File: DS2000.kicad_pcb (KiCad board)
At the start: 4 copper layers, 72 x 46 mm, 58 parts, among them J1 USB-C, J3 USB wire, SW1 MUTE, SW2 DEAFEN, SW3 DISCONNECT, U1 USBLC6-2SC6, U2 AP2112K-3.3, U3 RP2350A, U4 W25Q32JVSS, U5 74AHCT1G125, Y1 12MHz

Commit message: feat: cost-down for one-sided JLC assembly
Move every assembled part to the top side so JLC can assemble the board
with Economic PCBA, and swap parts that have a JLC basic (no feeder fee)
or cheaper drop-in equivalent.

- remove the USB-C receptacle (J1) and its CC resistors (R1, R2): the USB
  cable is soldered to J3, which now feeds +5V directly
- remove the PTC fuse (F1): the host port limits the current
- D1/D2: SK6812MINI-E reverse-mount (bottom) -> WS2812B-2020-V6 on the
  top, inside the Choc V1 LED window; no more board cut-outs
- C21/C22 move to the top, between the keys, under the keycap overhang
- U2: AP2112K-3.3 (SOT-23-5) -> XC6206P332MR (SOT-23-3, basic)
- Y1: ABM8-272-T3 -> YXC X322512MSB4SI (basic), C17/C18 15p -> 33p
- C3-C5 -> CL05A475MP5NRNC (basic), R5 -> 0402WGF330JTCE (basic)
- U1 -> UMW USBLC6-2SC6, U4 -> W25Q16JVSSIQ (2 MB, same footprint)
- the changed nets rerouted with Freerouting, existing tracks locked
- STEP model for the WS2812B-2020, docs and renders updated

Co-Authored-By: Claude Opus 5.5 <noreply@anthropic.com>
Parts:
- removed F1: 500mA hold, Fuse:Fuse_1206_3216Metric
- removed J1: USB-C, Connector_USB:USB_C_Receptacle_HRO_TYPE-C-31-M-12
- removed R1, R2: 5.1k, Resistor_SMD:R_0402_1005Metric
- C17, C18: value 15p -> 33p
- C21, C22: moved to F.Cu
- D1, D2: value SK6812MINI-E -> WS2812B-2020; footprint LED_SMD:LED_SK6812MINI-E_3.2x2.8mm_P1.5mm_ReverseMount -> LED_SMD:LED_WS2812B-2020_PLCC4_2.0x2.0mm; moved to F.Cu
- U2: value AP2112K-3.3 -> XC6206P332MR; footprint Package_TO_SOT_SMD:SOT-23-5 -> Package_TO_SOT_SMD:SOT-23-3
- moved C21 5.35 mm to (89.9, 105.7), turned to 90 degrees
- moved C22 5.35 mm to (107.9, 105.7), turned to 90 degrees
- turned D1 to 180 degrees
- turned D2 to 180 degrees
- turned U2 to 180 degrees
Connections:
- D1 pad 1: GND -> Net-(D1-DOUT)
- D1 pad 2: Net-(D1-DIN) -> GND
- D1 pad 3: +5V -> Net-(D1-DIN)
- D1 pad 4: Net-(D1-DOUT) -> +5V
- D2 pad 1: GND -> unconnected-(D2-DOUT-Pad1)
- D2 pad 2: Net-(D1-DOUT) -> GND
- D2 pad 3: +5V -> Net-(D1-DOUT)
- D2 pad 4: unconnected-(D2-DOUT-Pad4) -> +5V
- J3 pad 1: VBUS -> +5V
- U2 pad 1: +5V -> GND
- U2 pad 2: GND -> +3V3
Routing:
- net VBUS: track 83.9 -> 0.00 mm, vias 6 -> 0
- net +5V: track 96.9 -> 152.0 mm, vias 4 -> 7
- net /USB_CONN_DM: track 51.7 -> 31.4 mm, vias 2 -> 1
- net /USB_CONN_DP: track 34.0 -> 25.0 mm, vias 2 -> 1
- net Net-(J1-CC1): track 8.21 -> 0.00 mm, vias 1 -> 0
- net Net-(J1-CC2): track 7.35 -> 0.00 mm, vias 1 -> 0
- net Net-(D1-DOUT): track 13.2 -> 19.5 mm, vias 0 -> 2
- net Net-(D1-DIN): track 24.5 -> 22.6 mm, vias 1 -> 2
- net GND: track 26.1 -> 24.9 mm, vias 138 -> 136

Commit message: fix: U4 value matches the 2 MB flash
Co-Authored-By: Claude Opus 5.5 <noreply@anthropic.com>
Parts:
- U4: value W25Q32JVSS -> W25Q16JVSS
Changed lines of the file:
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@@
 			)
 		)
-		(property "Value" "W25Q32JVSS"
+		(property "Value" "W25Q16JVSS"
 			(at 0 3.6 0)
 			(layer "F.Fab")

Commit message: fix: keep the USB-C footprint, hand-soldered instead of assembled
The cost-down removed J1 to keep JLC's assembly one-sided. The receptacle
only has to stay out of JLC's files for that, not off the board: J1 is back
in its place on the bottom, marked DNP and excluded from the BOM and the
placement file, to be soldered by hand after assembly. J3 stays as the
alternative for a soldered cable.

- J1's VBUS goes straight to +5V, like J3; there is still no fuse.
- R1/R2, the 5.1k CC pull-downs a USB-C host needs before it supplies 5 V,
  are back on the top side (basic part, assembled).
- J1's escape routing is main's; the +5V and D+ runs it displaced were
  rerouted around it.
- set_fields.py, README and design notes describe J1 as DNP.

ERC 0. DRC: 0 unconnected, 0 parity issues; the rest is the 13 known
text_thickness notes and the two library-mismatch notes (Y1, and J1 as
on main).

Co-Authored-By: Claude Opus 5.5 <noreply@anthropic.com>
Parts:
- added J1: USB-C, Connector_USB:USB_C_Receptacle_HRO_TYPE-C-31-M-12, B.Cu at (100.0, 73.5)
- added R1: 5.1k, Resistor_SMD:R_0402_1005Metric, F.Cu at (93.3, 74.2)
- added R2: 5.1k, Resistor_SMD:R_0402_1005Metric, F.Cu at (106.7, 74.2)
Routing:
- net /USB_CONN_DM: track 31.4 -> 47.7 mm, vias 1 -> 2
- net /CC1: track 0.00 -> 8.21 mm, vias 0 -> 1
- net /USB_CONN_DP: track 25.0 -> 33.1 mm, vias 1 -> 2
- net /CC2: track 0.00 -> 7.35 mm, vias 0 -> 1
- net GND: track 24.9 -> 29.4 mm, vias 136 -> 137
- net +5V: track 152.0 -> 155.0 mm

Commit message: fix: back to the reference crystal, ABM8-272-T3 with 15 pF
JLC's design review flagged the basic YXC crystal against Raspberry Pi's
RP2350 hardware design guide. A crystal that does not start costs a whole
batch, against one extended-part fee: Y1 is the Abracon ABM8-272-T3 again
(C20625731, Economic PCBA) with 15 pF load caps (C1548), as the reference.

Co-Authored-By: Claude Opus 5.5 <noreply@anthropic.com>
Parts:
- C17, C18: value 33p -> 15p
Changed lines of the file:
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@@
 			)
 		)
-		(property "MPN" "X322512MSB4SI"
+		(property "MPN" "ABM8-272-T3"
 			(at 0 0 0)
 			(layer "F.Fab")
@@
 			)
 		)
-		(property "Manufacturer" "YXC"
+		(property "Manufacturer" "Abracon"
 			(at 0 0 0)
 			(layer "F.Fab")
@@
 			)
 		)
-		(property "LCSC" "C9002"
+		(property "LCSC" "C20625731"
 			(at 0 0 0)
 			(layer "F.Fab")
@@
 			)
 		)
-		(property "Value" "33p"
+		(property "Value" "15p"
 			(at 0 1.16 90)
 			(layer "F.Fab")
@@
 			)
 		)
-		(property "MPN" "0402CG330J500NT"
+		(property "MPN" "0402CG150J500NT"
 			(at 0 0 0)
 			(layer "F.Fab")
@@
 			)
 		)
-		(property "LCSC" "C1562"
+		(property "LCSC" "C1548"
 			(at 0 0 0)
 			(layer "F.Fab")
@@
 			)
 		)
-		(property "Value" "33p"
+		(property "Value" "15p"
 			(at 0 1.16 180)
 			(layer "F.Fab")
@@
 			)
 		)
-		(property "MPN" "0402CG330J500NT"
+		(property "MPN" "0402CG150J500NT"
 			(at 0 0 0)
 			(layer "F.Fab")
@@
 			)
 		)
-		(property "LCSC" "C1562"
+		(property "LCSC" "C1548"
 			(at 0 0 0)
 			(layer "F.Fab")

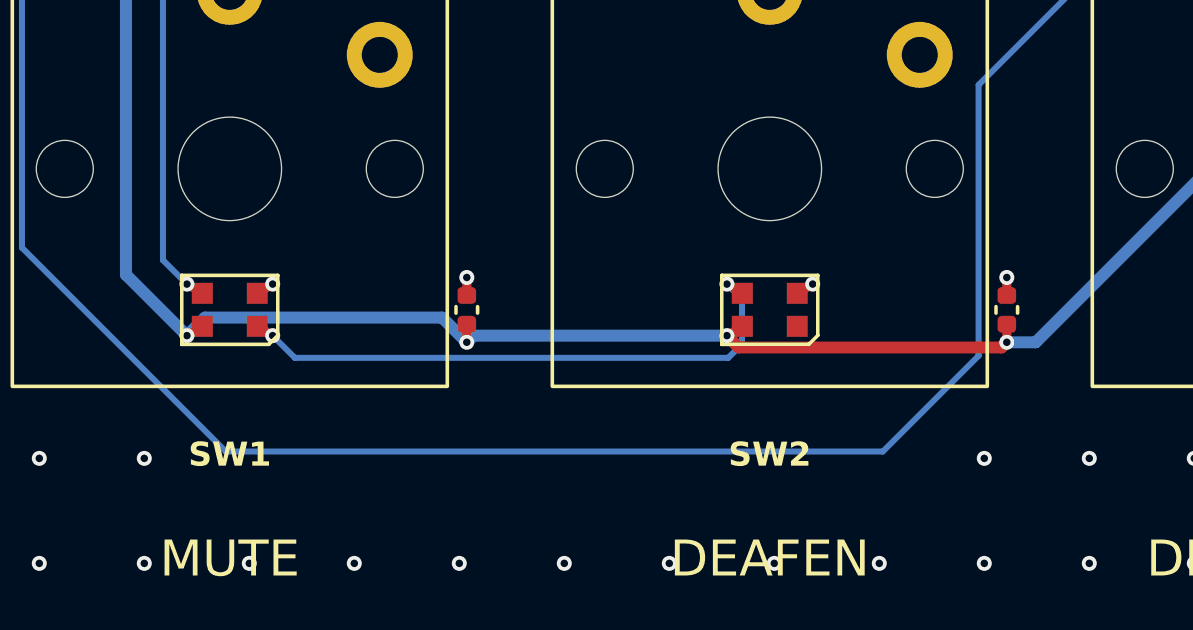
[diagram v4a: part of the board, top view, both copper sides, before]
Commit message: fix: SK6805-EC20 key LEDs, which JLC assembles in Economic PCBA
JLC's order review reported the WS2812B-2020 (C52917434) as Standard-PCBA
only, which brings back the setup fee and a 70 mm minimum board side. The
OPSCO SK6805-EC20 (C2890036) is the same 2.0 x 2.0 mm top-emitting,
WS2812-compatible part (800 kHz, GRB), assembles in Economic, and is
thinner: 0.65 mm instead of 0.84, more room under the Choc V1 housing.

- Its pinout (1 VDD, 2 DOUT, 3 GND, 4 DIN) is not in KiCad's library, so
  the project gets its own symbol library (DS2000.kicad_sym, sym-lib-table)
  and footprint (datasheet land pattern: 0.8 x 0.7 mm pads), plus a STEP
  model from gen_models.py.
- Turned 270 deg, every net keeps its corner: the routing only follows the
  pads, and the +5V run under D2 moves 0.2 mm down to clear the longer pads.
- DIN needs 0.7 x VDD, so U5's level shifter is now required.
- 5 mA per colour, about half a WS2812B: to confirm through a keycap.

ERC 0. DRC: 0 unconnected, 0 parity issues; the known 15 notes only.

Co-Authored-By: Claude Opus 5.5 <noreply@anthropic.com>
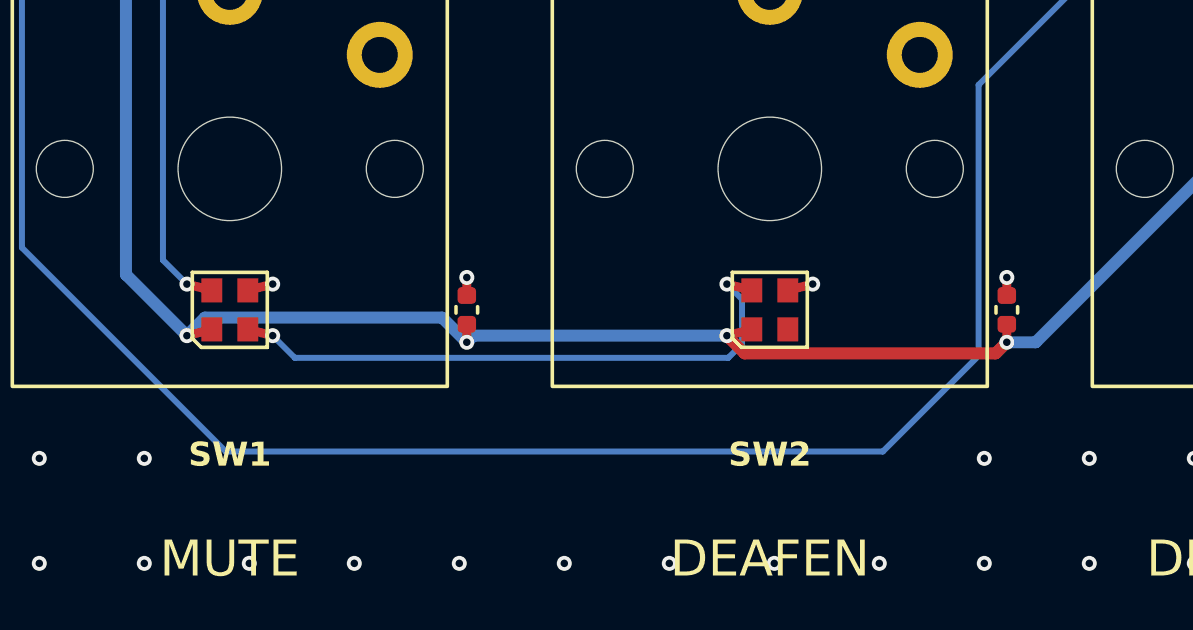
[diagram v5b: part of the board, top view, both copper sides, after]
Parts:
- D1, D2: value WS2812B-2020 -> SK6805-EC20; footprint LED_SMD:LED_WS2812B-2020_PLCC4_2.0x2.0mm -> DS2000:LED_SK6805-EC20_2.0x2.0mm
- turned D1 to -90 degrees
- turned D2 to -90 degrees
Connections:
- D1 pad 1: Net-(D1-DOUT) -> +5V
- D1 pad 2: GND -> Net-(D1-DOUT)
- D1 pad 3: Net-(D1-DIN) -> GND
- D1 pad 4: +5V -> Net-(D1-DIN)
- D2 pad 1: unconnected-(D2-DOUT-Pad1) -> +5V
- D2 pad 2: GND -> unconnected-(D2-DOUT-Pad2)
- D2 pad 3: Net-(D1-DOUT) -> GND
- D2 pad 4: +5V -> Net-(D1-DOUT)
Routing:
- net +5V: track 155.0 -> 155.7 mm
- net Net-(D1-DOUT): track 19.5 -> 20.1 mm
- net GND: track 29.4 -> 30.0 mm

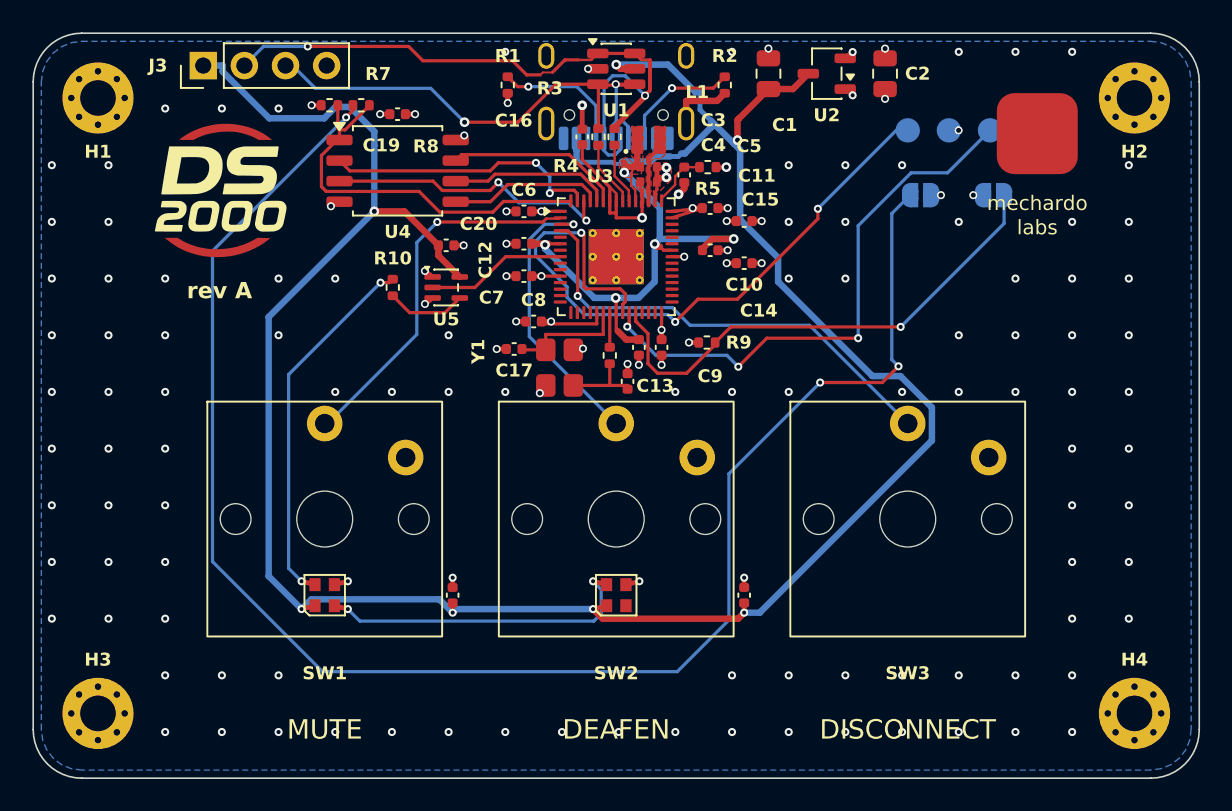
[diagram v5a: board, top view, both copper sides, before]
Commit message: feat: production review changes to the board and schematic
- U4: 4 MB flash (W25Q32JVSSIQ, C82344), the RP2350-Zero's size, room for
  A/B firmware updates
- C1/C2: 10u -> 4.7u (CL21A475KAQNNNE, C1779, basic), so VBUS stays near
  USB 2.0's 10 uF
- J1 is no longer DNP: a `Config` field (+standard) lets the KiBot variant
  decide whether JLC fits it (standard) or it is soldered by hand (economic)
- J3: four SMD wire pads on the bottom beside J1 (WirePads_1x04_P2.54mm_SMD)
  instead of through holes on the visible face; its USB branch drops from
  ~20 mm to ~12 mm per line
- USB pair from J3 to U1 hand-routed as a coupled pair, 0.25 mm / 0.15 mm
  (~90 ohm on JLC04161H-7628); USB net class updated to match
- R1 moves below the pair, CC1 via moved with it
- BOOTSEL (R8 -> JP1): 95 mm -> 53 mm, three vias, kept clear of J1's shell
- TP4-TP6: production test pads for +5V, +3V3 and +1V1 on the bottom, new
  stage in the schematic
- F.Cu GND pour restored (lost in 56300c4); both logos' exposed copper is
  now a GND pad, so it no longer floats on the touchable face
- JLCJLCJLCJLC on B.SilkS, so JLC's order number goes underneath
- title blocks: DS2000, 2026-10-23, current LEDs

ERC 0; DRC 0 errors, 0 unconnected, schematic parity clean (known warnings:
TrueType text thickness, J1/Y1 footprints edited on the board).

Co-Authored-By: Claude Opus 5.5 <noreply@anthropic.com>
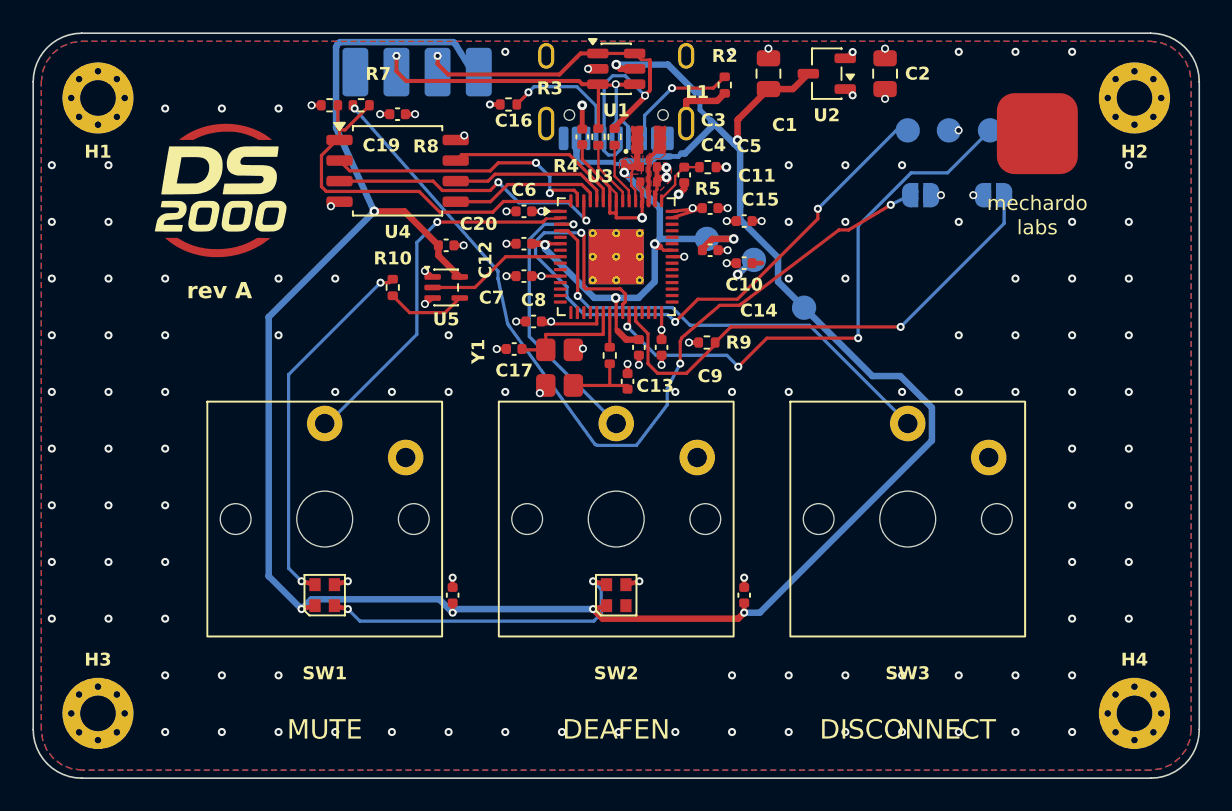
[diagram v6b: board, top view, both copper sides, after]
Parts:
- added TP4: +5V, TestPoint:TestPoint_Pad_D1.5mm, B.Cu at (111.6, 88.0)
- added TP5: +3V3, TestPoint:TestPoint_Pad_D1.5mm, B.Cu at (108.5, 85.0)
- added TP6: +1V1, TestPoint:TestPoint_Pad_D1.5mm, B.Cu at (105.6, 83.7)
- C1, C2: value 10u -> 4.7u
- J3: footprint Connector_PinHeader_2.54mm:PinHeader_1x04_P2.54mm_Vertical -> DS2000:WirePads_1x04_P2.54mm_SMD; moved to B.Cu
- U4: value W25Q16JVSS -> W25Q32JVSS
- moved J3 13.2 mm to (87.7, 73.4), turned to 180 degrees
- moved R1 1.20 mm to (93.3, 75.4), turned to 0 degrees
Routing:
- net Net-(JP1-B): track 101.2 -> 53.2 mm
- net /USB_CONN_DM: track 47.7 -> 35.3 mm
- net /USB_CONN_DP: track 33.1 -> 25.1 mm
- net +5V: track 155.7 -> 158.7 mm
- net +3V3: track 33.7 -> 35.1 mm, vias 16 -> 17
- net GND: vias 137 -> 136
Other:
- board text added: "1V1"
- board text added: "3V3"
- board text added: "5V"
- board text added: "D+"
- board text added: "D-"
- board text added: "JLCJLCJLCJLC"
